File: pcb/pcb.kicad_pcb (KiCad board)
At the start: 2 copper layers, 1 part, among them J1 TYPE-C-31-M-31

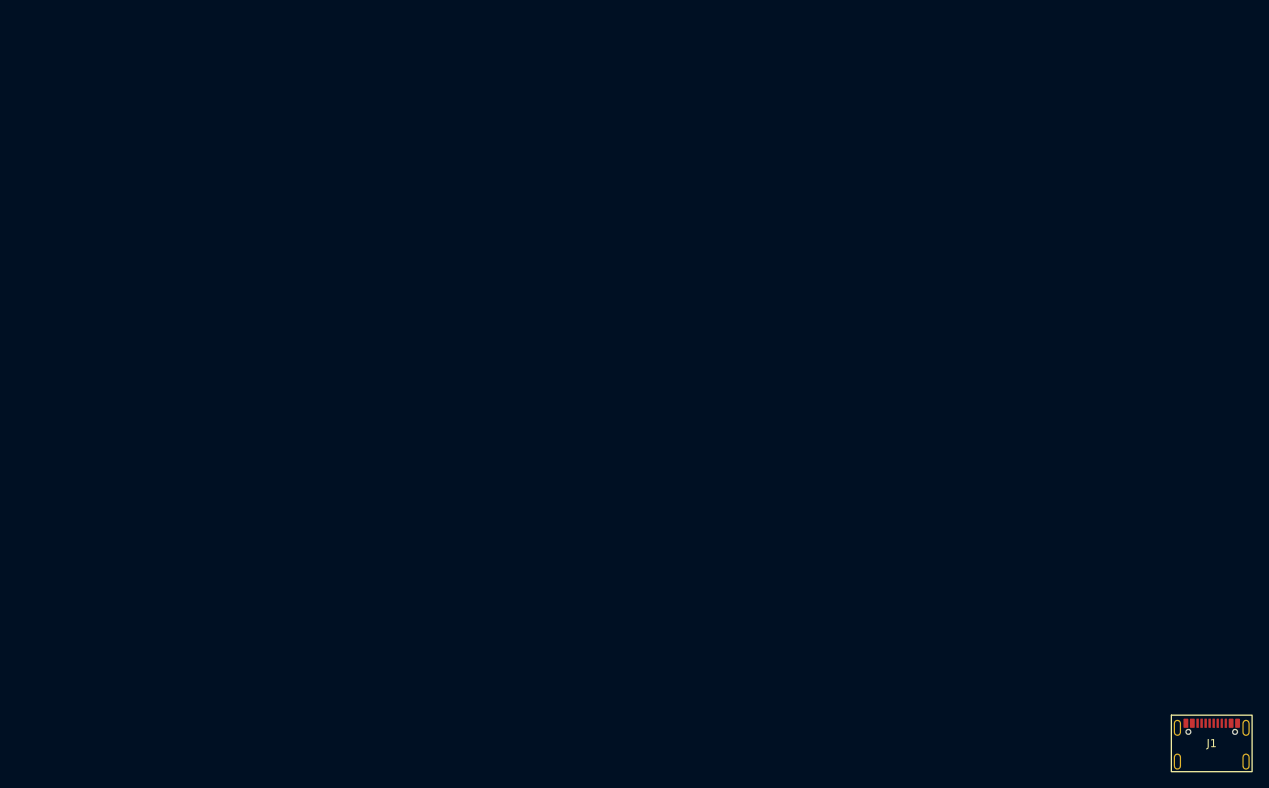
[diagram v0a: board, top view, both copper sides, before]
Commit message: started working on voltage regulator
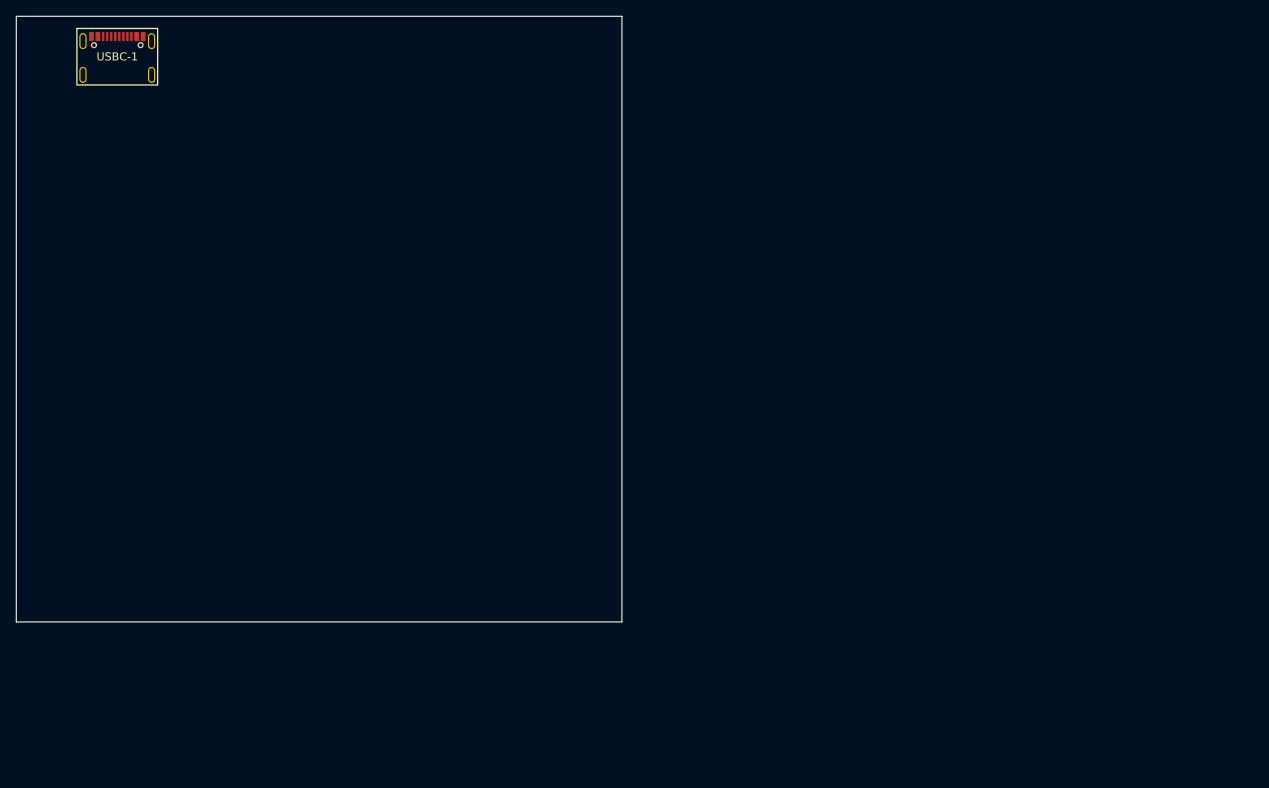
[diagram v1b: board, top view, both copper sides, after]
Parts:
- removed J1: TYPE-C-31-M-31, Andrews_Library:LCSC_SMD_USBC_C2760486
- added USBC-1: TYPE-C-31-M-31, Andrews_Library:LCSC_SMD_USBC_C2760486, F.Cu at (12.5, 5.00)
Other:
- board outline added: 75 x 75 mm
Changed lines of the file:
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@@
 	(footprint "Andrews_Library:LCSC_SMD_USBC_C2760486"
 		(layer "F.Cu")
-		(at 148.05 90.05)
-		(property "Reference" "J1"
+		(at 12.5 5)
+		(property "Reference" "USBC-1"
 			(at 0 0 0)
 			(unlocked yes)
@@
 			(layers "*.Cu" "*.Mask")
 			(remove_unused_layers no)
-			(net "unconnected-(J1-Pad1)_1")
+			(net "unconnected-(USBC-1-Pad1)_2")
 			(pinfunction "1_1")
 			(pintype "passive+no_connect")
@@
 			(layers "*.Cu" "*.Mask")
 			(remove_unused_layers no)
-			(net "unconnected-(J1-Pad1)_3")
+			(net "unconnected-(USBC-1-Pad1)_1")
 			(pinfunction "1_1")
 			(pintype "passive+no_connect")
@@
 			(layers "*.Cu" "*.Mask")
 			(remove_unused_layers no)
-			(net "unconnected-(J1-Pad1)")
+			(net "unconnected-(USBC-1-Pad1)_3")
 			(pinfunction "1_1")
 			(pintype "passive+no_connect")
@@
 			(layers "*.Cu" "*.Mask")
 			(remove_unused_layers no)
-			(net "unconnected-(J1-Pad1)_2")
+			(net "unconnected-(USBC-1-Pad1)")
 			(pinfunction "1_1")
 			(pintype "passive+no_connect")
@@
 			(layers "F.Cu" "F.Mask" "F.Paste")
 			(roundrect_rratio 0.15)
-			(net "unconnected-(J1-CC1-PadA5)")
+			(net "unconnected-(USBC-1-CC1-PadA5)")
 			(pinfunction "CC1_A5")
 			(pintype "bidirectional+no_connect")
@@
 			(layers "F.Cu" "F.Mask" "F.Paste")
 			(roundrect_rratio 0.15)
-			(net "unconnected-(J1-DP1-PadA6)")
+			(net "unconnected-(USBC-1-DP1-PadA6)")
 			(pinfunction "DP1_A6")
 			(pintype "bidirectional+no_connect")
@@
 			(layers "F.Cu" "F.Mask" "F.Paste")
 			(roundrect_rratio 0.15)
-			(net "unconnected-(J1-DN1-PadA7)")
+			(net "unconnected-(USBC-1-DN1-PadA7)")
 			(pinfunction "DN1_A7")
 			(pintype "bidirectional+no_connect")
@@
 			(layers "F.Cu" "F.Mask" "F.Paste")
 			(roundrect_rratio 0.15)
-			(net "unconnected-(J1-SBU1-PadA8)")
+			(net "unconnected-(USBC-1-SBU1-PadA8)")
 			(pinfunction "SBU1_A8")
 			(pintype "bidirectional+no_connect")
@@
 			(layers "F.Cu" "F.Mask" "F.Paste")
 			(roundrect_rratio 0.15)
-			(net "unconnected-(J1-CC2-PadB5)")
+			(net "unconnected-(USBC-1-CC2-PadB5)")
 			(pinfunction "CC2_B5")
 			(pintype "bidirectional+no_connect")
@@
 			(layers "F.Cu" "F.Mask" "F.Paste")
 			(roundrect_rratio 0.15)
-			(net "unconnected-(J1-DP2-PadB6)")
+			(net "unconnected-(USBC-1-DP2-PadB6)")
 			(pinfunction "DP2_B6")
 			(pintype "bidirectional+no_connect")
@@
 			(layers "F.Cu" "F.Mask" "F.Paste")
 			(roundrect_rratio 0.15)
-			(net "unconnected-(J1-DN2-PadB7)")
+			(net "unconnected-(USBC-1-DN2-PadB7)")
 			(pinfunction "DN2_B7")
 			(pintype "bidirectional+no_connect")
@@
 			(layers "F.Cu" "F.Mask" "F.Paste")
 			(roundrect_rratio 0.15)
-			(net "unconnected-(J1-SBU2-PadB8)")
+			(net "unconnected-(USBC-1-SBU2-PadB8)")
 			(pinfunction "SBU2_B8")
 			(pintype "bidirectional+no_connect")
@@
 		(embedded_fonts no)
 	)
+	(gr_rect
+		(start 0 0)
+		(end 25 25)
+		(stroke
+			(width 0.1)
+			(type solid)
+		)
+		(fill no)
+		(layer "Dwgs.User")
+	)
+	(gr_rect
+		(start 0 25)
+		(end 25 50)
+		(stroke
+			(width 0.1)
+			(type solid)
+		)
+		(fill no)
+		(layer "Dwgs.User")
+	)
+	(gr_rect
+		(start 0 50)
+		(end 25 75)
+		(stroke
+			(width 0.1)
+			(type solid)
+		)
+		(fill no)
+		(layer "Dwgs.User")
+	)
+	(gr_rect
+		(start 25 0)
+		(end 50 25)
+		(stroke
+			(width 0.1)
+			(type solid)
+		)
+		(fill no)
+		(layer "Dwgs.User")
+	)
+	(gr_rect
+		(start 25 25)
+		(end 50 50)
+		(stroke
+			(width 0.1)
+			(type solid)
+		)
+		(fill no)
+		(layer "Dwgs.User")
+	)
+	(gr_rect
+		(start 25 50)
+		(end 50 75)
+		(stroke
+			(width 0.1)
+			(type solid)
+		)
+		(fill no)
+		(layer "Dwgs.User")
+	)
+	(gr_rect
+		(start 50 0)
+		(end 75 25)
+		(stroke
+			(width 0.1)
+			(type solid)
+		)
+		(fill no)
+		(layer "Dwgs.User")
+	)
+	(gr_rect
+		(start 50 25)
+		(end 75 50)
+		(stroke
+			(width 0.1)
+			(type solid)
+		)
+		(fill no)
+		(layer "Dwgs.User")
+	)
+	(gr_rect
+		(start 50 50)
+		(end 75 75)
+		(stroke
+			(width 0.1)
+			(type solid)
+		)
+		(fill no)
+		(layer "Dwgs.User")
+	)
+	(gr_rect
+		(start 0 0)
+		(end 75 75)
+		(stroke
+			(width 0.05)
+			(type solid)
+		)
+		(fill no)
+		(layer "Edge.Cuts")
+	)
 	(embedded_fonts no)

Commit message: added it to the pcb
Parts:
- added U1: 1117-3.3, Andrews_Library:LCSC_SMD_1117-3.3v_C5125088, F.Cu at (25.6, 8.55)
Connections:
- USBC-1 pad 1: unconnected-(USBC-1-Pad1) -> GND
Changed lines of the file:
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@@
 			(layers "*.Cu" "*.Mask")
 			(remove_unused_layers no)
-			(net "unconnected-(USBC-1-Pad1)_2")
+			(net "GND")
 			(pinfunction "1_1")
-			(pintype "passive+no_connect")
+			(pintype "passive")
 		)
 		(pad "1" thru_hole oval
@@
 			(layers "*.Cu" "*.Mask")
 			(remove_unused_layers no)
-			(net "unconnected-(USBC-1-Pad1)_1")
+			(net "GND")
 			(pinfunction "1_1")
-			(pintype "passive+no_connect")
+			(pintype "passive")
 		)
 		(pad "1" thru_hole oval
@@
 			(layers "*.Cu" "*.Mask")
 			(remove_unused_layers no)
-			(net "unconnected-(USBC-1-Pad1)_3")
+			(net "GND")
 			(pinfunction "1_1")
-			(pintype "passive+no_connect")
+			(pintype "passive")
 		)
 		(pad "1" thru_hole oval
@@
 			(layers "*.Cu" "*.Mask")
 			(remove_unused_layers no)
-			(net "unconnected-(USBC-1-Pad1)")
+			(net "GND")
 			(pinfunction "1_1")
-			(pintype "passive+no_connect")
+			(pintype "passive")
 		)
 		(pad "A1/B12" smd roundrect
@@
 		)
 		(embedded_fonts no)
+	)
+	(footprint "Andrews_Library:LCSC_SMD_1117-3.3v_C5125088"
+		(layer "F.Cu")
+		(at 25.55 8.55)
+		(property "Reference" "U1"
+			(at 0 -3.25 0)
+			(unlocked yes)
+			(layer "F.SilkS")
+			(effects
+				(font
+					(size 1 1)
+					(thickness 0.1)
+				)
+			)
+		)
+		(property "Value" "1117-3.3"
+			(at 0 3.9 0)
+			(unlocked yes)
+			(layer "F.Fab")
+			(effects
+				(font
+					(size 1 1)
+					(thickness 0.15)
+				)
+			)
+		)
+		(property "Datasheet" "https://www.lcsc.com/datasheet/C5125088.pdf"
+			(at 0 0 0)
+			(unlocked yes)
+			(layer "F.Fab")
+			(hide yes)
+			(effects
+				(font
+					(size 1 1)
+					(thickness 0.15)
+				)
+			)
+		)
+		(property "Description" ""
+			(at 0 0 0)
+			(unlocked yes)
+			(layer "F.Fab")
+			(hide yes)
+			(effects
+				(font
+					(size 1 1)
+					(thickness 0.15)
+				)
+			)
+		)
+		(property "LCSC" "C5125088"
+			(at 0 0 0)
+			(unlocked yes)
+			(layer "F.Fab")
+			(hide yes)
+			(effects
+				(font
+					(size 1 1)
+					(thickness 0.15)
+				)
+			)
+		)
+		(sheetname "/")
+		(sheetfile "pcb.kicad_sch")
+		(units
+			(unit
+				(name "A")
+				(pins "3" "1" "2")
+			)
+		)
+		(attr smd)
+		(duplicate_pad_numbers_are_jumpers no)
+		(fp_rect
+			(start -3.5 -7.5)
+			(end 3.5 1)
+			(stroke
+				(width 0.1)
+				(type solid)
+			)
+			(fill no)
+			(layer "F.SilkS")
+		)
+		(fp_rect
+			(start -2.95 -5)
+			(end 2.95 -1.5)
+			(stroke
+				(width 0.1)
+				(type solid)
+			)
+			(fill no)
+			(layer "F.SilkS")
+		)
+		(fp_text user "${REFERENCE}"
+			(at 0 2.1 0)
+			(unlocked yes)
+			(layer "F.Fab")
+			(effects
+				(font
+					(size 1 1)
+					(thickness 0.15)
+				)
+			)
+		)
+		(pad "1" smd roundrect
+			(at -2.3 0)
+			(size 0.9 1.1)
+			(layers "F.Cu" "F.Mask" "F.Paste")
+			(roundrect_rratio 0.15)
+			(net "GND")
+			(pinfunction "GND/ADJ_1")
+			(pintype "power_in")
+		)
+		(pad "2" smd roundrect
+			(at 0 -6.45)
+			(size 3.2 1.1)
+			(layers "F.Cu" "F.Mask" "F.Paste")
+			(roundrect_rratio 0.15)
+			(net "VBUS")
+			(pinfunction "VOUT_2")
+			(pintype "power_out")
+		)
+		(pad "2" smd roundrect
+			(at 0 0)
+			(size 0.9 1.1)
+			(layers "F.Cu" "F.Mask" "F.Paste")
+			(roundrect_rratio 0.15)
+			(net "VBUS")
+			(pinfunction "VOUT_2")
+			(pintype "power_out")
+		)
+		(pad "3" smd roundrect
+			(at 2.3 0)
+			(size 0.9 1.1)
+			(layers "F.Cu" "F.Mask" "F.Paste")
+			(roundrect_rratio 0.15)
+			(net "Net-(U1-VIN)")
+			(pinfunction "VIN_3")
+			(pintype "power_in")
+		)
+		(zone
+			(layer "F.SilkS")
+			(hatch edge 0.5)
+			(connect_pads
+				(clearance 0)
+			)
+			(min_thickness 0.25)
+			(keepout
+				(tracks allowed)
+				(vias allowed)
+				(pads allowed)
+				(copperpour allowed)
+				(footprints not_allowed)
+			)
+			(placement
+				(enabled no)
+				(sheetname "")
+			)
+			(fill
+				(thermal_gap 0.5)
+				(thermal_bridge_width 0.5)
+				(island_removal_mode 0)
+			)
+			(polygon
+				(pts
+					(xy 22.05 1.05) (xy 29.05 1.05) (xy 29.05 9.55) (xy 22.05 9.55)
+				)
+			)
+		)
+		(embedded_fonts no)

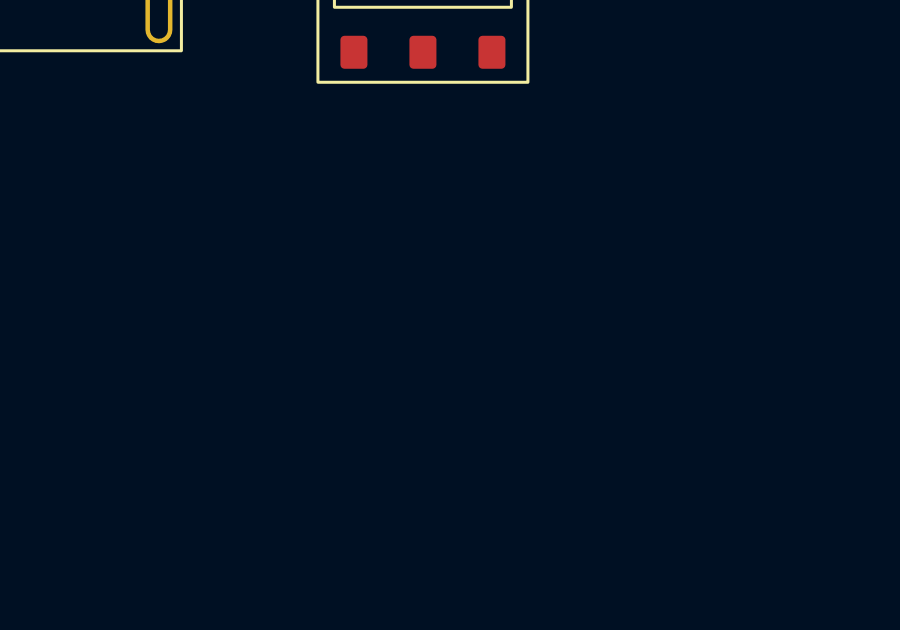
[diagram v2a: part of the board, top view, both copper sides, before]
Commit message: added footprints to c
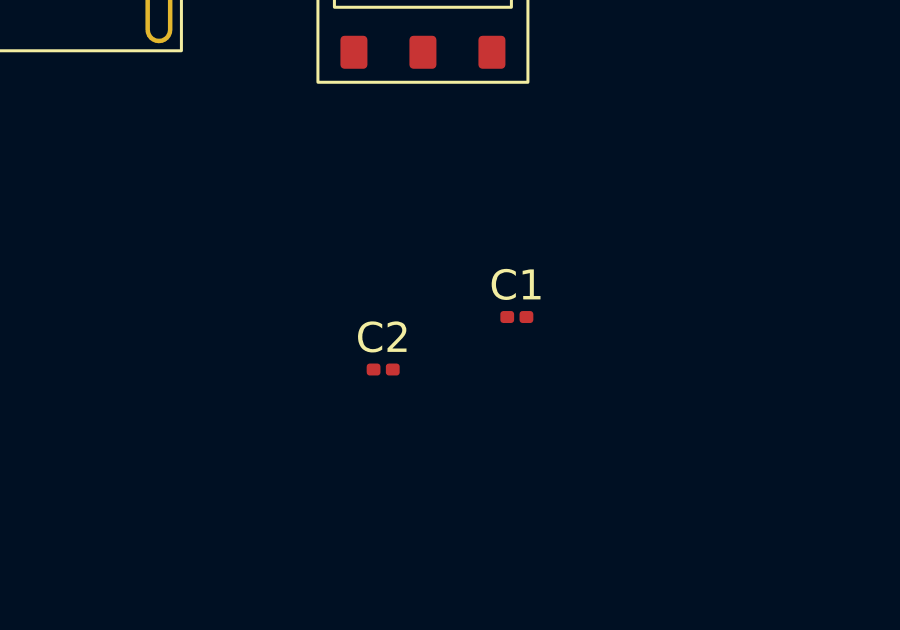
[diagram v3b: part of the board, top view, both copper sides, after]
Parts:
- added C1: 10uF, Capacitor_SMD:C_0201_0603Metric, F.Cu at (28.7, 17.4)
- added C2: 10uF, Capacitor_SMD:C_0201_0603Metric, F.Cu at (24.2, 19.1)

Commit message: wired some stuff
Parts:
- moved C2 10.7 mm to (34.8, 17.5), turned to -90 degrees
- moved U1 9.83 mm to (32.5, 15.5)
- moved C1 3.82 mm to (32.5, 17.5), turned to 90 degrees
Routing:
- net VBUS: track 0.00 -> 1.68 mm
- net Net-(U1-VIN): track 0.00 -> 1.68 mm
- added copper zone on F.Cu, net GND
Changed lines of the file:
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@@
 	(footprint "Capacitor_SMD:C_0201_0603Metric"
 		(layer "F.Cu")
-		(at 28.68 17.375)
+		(at 32.5 17.5 90)
 		(descr "Capacitor SMD 0201 (0603 Metric), square (rectangular) end terminal, IPC-7351 nominal, (Body size source: https://www.vishay.com/docs/20052/crcw0201e3.pdf)")
 		(tags "capacitor")
 		(property "Reference" "C1"
-			(at 0 -1.05 0)
-			(layer "F.SilkS")
-			(effects
-				(font
-					(size 1 1)
-					(thickness 0.15)
+			(at -1.2 0 180)
+			(layer "F.SilkS")
+			(effects
+				(font
+					(size 0.5 0.5)
+					(thickness 0.125)
 				)
 			)
 		)
 		(property "Value" "10uF"
-			(at 0 1.05 0)
-			(layer "F.Fab")
-			(effects
-				(font
-					(size 1 1)
-					(thickness 0.15)
+			(at 0 1.05 90)
+			(layer "F.Fab")
+			(hide yes)
+			(effects
+				(font
+					(size 0.5 0.5)
+					(thickness 0.125)
 				)
 			)
 		)
 		(property "Datasheet" ""
-			(at 0 0 0)
+			(at 0 0 90)
 			(layer "F.Fab")
 			(hide yes)
@@
 		)
 		(property "Description" "Unpolarized capacitor"
-			(at 0 0 0)
+			(at 0 0 90)
 			(layer "F.Fab")
 			(hide yes)
@@
 		)
 		(property "KiLib_Generator" "SMD_2terminal_chip_molded"
-			(at 0 0 0)
+			(at 0 0 90)
 			(layer "F.SilkS")
 			(hide yes)
@@
 		)
 		(property "LCSC" "C1691"
-			(at 0 0 0)
+			(at 0 0 90)
 			(unlocked yes)
 			(layer "F.Fab")
@@
 		)
 		(fp_text user "${REFERENCE}"
-			(at 0 -0.68 0)
+			(at 0 0 90)
 			(layer "F.Fab")
 			(effects
@@
 		)
 		(pad "" smd roundrect
-			(at -0.345 0)
+			(at -0.345 0 90)
 			(size 0.318 0.36)
 			(layers "F.Paste")
@@
 		)
 		(pad "" smd roundrect
-			(at 0.345 0)
+			(at 0.345 0 90)
 			(size 0.318 0.36)
 			(layers "F.Paste")
@@
 		)
 		(pad "1" smd roundrect
-			(at -0.32 0)
+			(at -0.32 0 90)
 			(size 0.46 0.4)
 			(layers "F.Cu" "F.Mask")
@@
 		)
 		(pad "2" smd roundrect
-			(at 0.32 0)
+			(at 0.32 0 90)
 			(size 0.46 0.4)
 			(layers "F.Cu" "F.Mask")
@@
 	(footprint "Andrews_Library:LCSC_SMD_1117-3.3v_C5125088"
 		(layer "F.Cu")
-		(at 25.55 8.55)
+		(at 32.5 15.5)
 		(property "Reference" "U1"
 			(at 0 -3.25 0)
@@
 		)
 		(property "Value" "1117-3.3"
-			(at 0 3.9 0)
+			(at 0 -8.7 0)
 			(unlocked yes)
 			(layer "F.Fab")
@@
 		)
 		(fp_text user "${REFERENCE}"
-			(at 0 2.1 0)
+			(at 0 -10.5 0)
 			(unlocked yes)
 			(layer "F.Fab")
@@
 			(polygon
 				(pts
-					(xy 22.05 1.05) (xy 29.05 1.05) (xy 29.05 9.55) (xy 22.05 9.55)
+					(xy 29 8) (xy 36 8) (xy 36 16.5) (xy 29 16.5)
 				)
 			)
@@
 	(footprint "Capacitor_SMD:C_0201_0603Metric"
 		(layer "F.Cu")
-		(at 24.225 19.125)
+		(at 34.8 17.5 -90)
 		(descr "Capacitor SMD 0201 (0603 Metric), square (rectangular) end terminal, IPC-7351 nominal, (Body size source: https://www.vishay.com/docs/20052/crcw0201e3.pdf)")
 		(tags "capacitor")
 		(property "Reference" "C2"
-			(at 0 -1.05 0)
-			(layer "F.SilkS")
-			(effects
-				(font
-					(size 1 1)
-					(thickness 0.15)
+			(at 1.2 0 0)
+			(layer "F.SilkS")
+			(effects
+				(font
+					(size 0.5 0.5)
+					(thickness 0.125)
 				)
 			)
 		)
 		(property "Value" "10uF"
-			(at 0 1.05 0)
-			(layer "F.Fab")
-			(effects
-				(font
-					(size 1 1)
-					(thickness 0.15)
+			(at 0 1.05 90)
+			(layer "F.Fab")
+			(hide yes)
+			(effects
+				(font
+					(size 0.5 0.5)
+					(thickness 0.125)
 				)
 			)
 		)
 		(property "Datasheet" ""
-			(at 0 0 0)
+			(at 0 0 90)
 			(layer "F.Fab")
 			(hide yes)
@@
 		)
 		(property "Description" "Unpolarized capacitor"
-			(at 0 0 0)
+			(at 0 0 90)
 			(layer "F.Fab")
 			(hide yes)
@@
 		)
 		(property "KiLib_Generator" "SMD_2terminal_chip_molded"
-			(at 0 0 0)
+			(at 0 0 90)
 			(layer "F.SilkS")
 			(hide yes)
@@
 		)
 		(property "LCSC" "C1691"
-			(at 0 0 0)
+			(at 0 0 270)
 			(unlocked yes)
 			(layer "F.Fab")
@@
 		)
 		(fp_text user "${REFERENCE}"
-			(at 0 -0.68 0)
+			(at 0 -0.05 90)
 			(layer "F.Fab")
 			(effects
@@
 		)
 		(pad "" smd roundrect
-			(at -0.345 0)
+			(at -0.345 0 270)
 			(size 0.318 0.36)
 			(layers "F.Paste")
@@
 		)
 		(pad "" smd roundrect
-			(at 0.345 0)
+			(at 0.345 0 270)
 			(size 0.318 0.36)
 			(layers "F.Paste")
@@
 		)
 		(pad "1" smd roundrect
-			(at -0.32 0)
+			(at -0.32 0 270)
 			(size 0.46 0.4)
 			(layers "F.Cu" "F.Mask")
@@
 		)
 		(pad "2" smd roundrect
-			(at 0.32 0)
+			(at 0.32 0 270)
 			(size 0.46 0.4)
 			(layers "F.Cu" "F.Mask")
@@
 		(layer "Edge.Cuts")
 	)
+	(segment
+		(start 32.5 15.5)
+		(end 32.5 17.18)
+		(width 0.2)
+		(layer "F.Cu")
+		(net "VBUS")
+	)
+	(segment
+		(start 34.8 15.5)
+		(end 34.8 17.18)
+		(width 0.2)
+		(layer "F.Cu")
+		(net "Net-(U1-VIN)")
+	)
+	(zone
+		(net "GND")
+		(layer "F.Cu")
+		(hatch edge 0.5)
+		(connect_pads
+			(clearance 0.5)
+		)
+		(min_thickness 0.25)
+		(fill yes
+			(thermal_gap 0.5)
+			(thermal_bridge_width 0.5)
+			(island_removal_mode 0)
+		)
+		(polygon
+			(pts
+				(xy 75 0) (xy 0 0) (xy 0 75) (xy 75 75)
+			)
+		)
+	)
+	(group ""
+		(members "4c363494-5d20-44a3-9b12-37bc64127a15" "7ff470fd-2abd-486a-b746-3b467e71a7f8"
+			"a43b688b-cef3-4c08-969a-ef6623efc0b7" "c16a55e6-c9ba-4bf5-9418-845e8fc3c2c0"
+			"e2951551-5bd3-452b-943a-e5c31ddf3bfe"
+		)
+	)
 	(embedded_fonts no)
